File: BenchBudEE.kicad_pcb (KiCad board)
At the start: 4 copper layers, 165.1 x 63.5 mm, 67 parts, among them K1 1461069-5, P1 24 Pin MiniFit JR, P2 CONN_3X2, P3 CONN_2, P4 12 Pin Terminal Block, P5 3 Pin TB, Q1 2N3904, Q2 DMN65D8L-7, Q3 AOD476, Q4 AOD476, U1 LTV-816S, U2 MCP3901, U3 LMT84, U4 OPA4170, U6 MCP4801

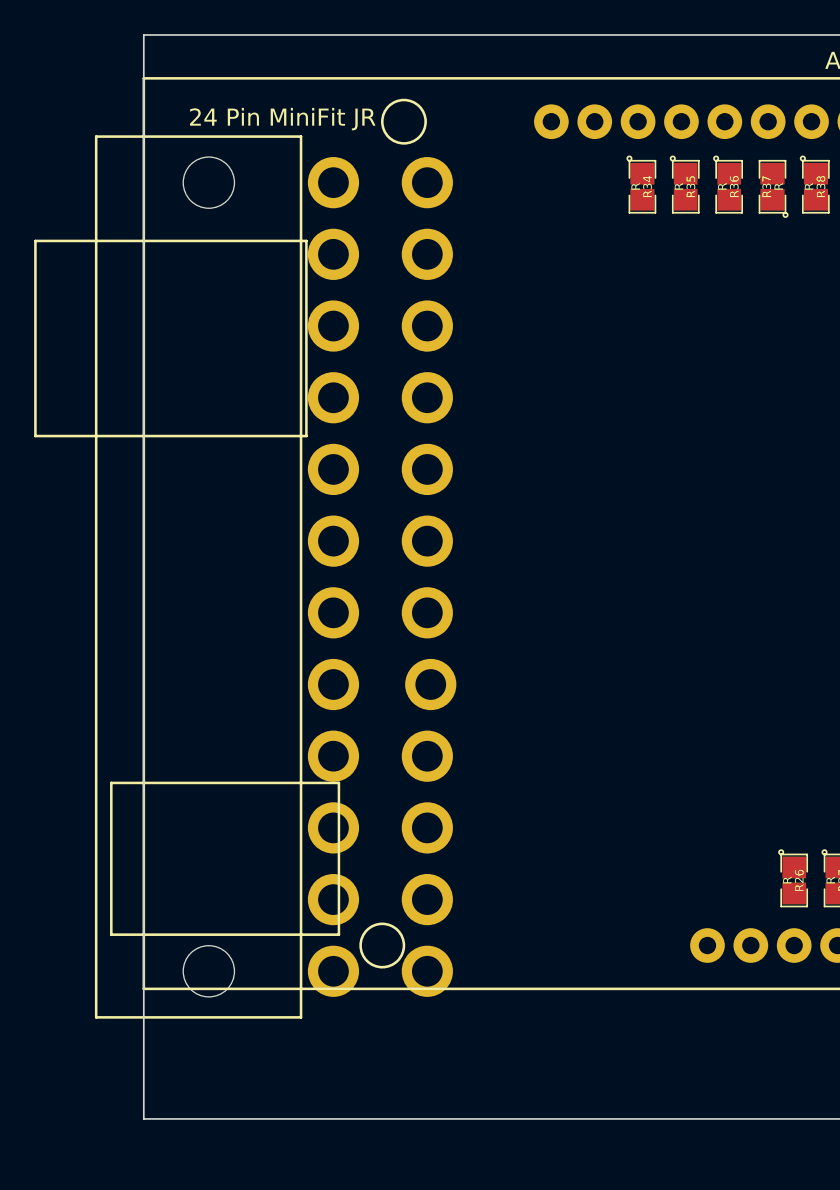
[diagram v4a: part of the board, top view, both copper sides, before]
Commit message: Power protection and filter: assc/placement
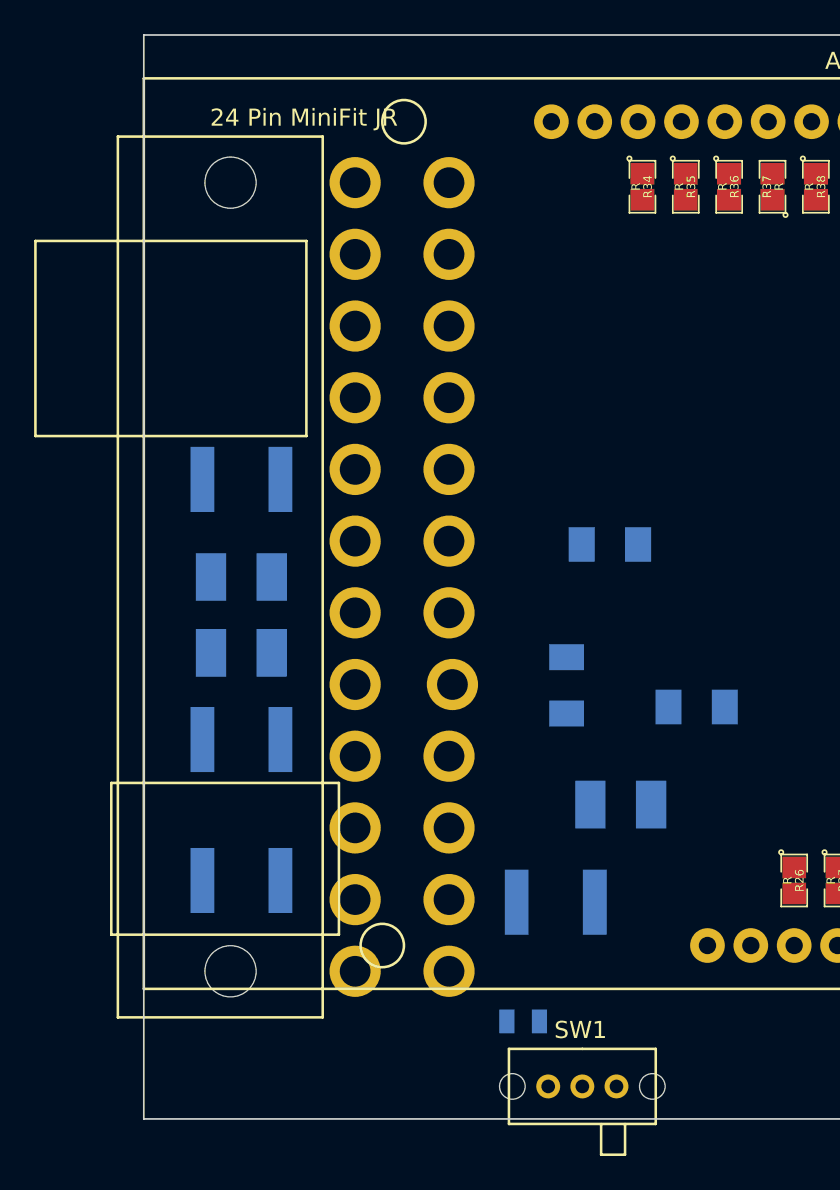
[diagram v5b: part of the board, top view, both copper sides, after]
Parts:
- added C2: C, SM1206, B.Cu at (149.2, 141.6)
- added C3: C, SM1206, B.Cu at (146.7, 149.9)
- added C4: C, SM1206, B.Cu at (154.3, 151.1)
- added L1: CM322522-220KL, SM1210L, B.Cu at (127.6, 148.0)
- added L2: CM322522-220KL, SM1210L, B.Cu at (127.6, 143.5)
- added L3: CM322522-220KL, SM1210L, B.Cu at (149.9, 156.8)
- added R14: R, SM0805, B.Cu at (144.1, 169.5)
- added SW1: Power Switch, BB_switch, F.Cu at (143.5, 173.4)
- added TH1: MINISMDC050F-2, SM1812, B.Cu at (127.6, 161.3)
- added TH2: MINISMDC050F-2, SM1812, B.Cu at (127.6, 153.0)
- added TH3: MINISMDC050F-2, SM1812, B.Cu at (127.6, 137.8)
- added TH4: MINISMDC050F-2, SM1812, B.Cu at (146.1, 162.6)
- moved P1 1.27 mm to (127.0, 143.5)

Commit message: Power Adjustment: assc/placement
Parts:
- added C14: C, SM0805, F.Cu at (189.9, 145.4)
- added C15: C, SM0805, F.Cu at (189.9, 127.0)
- added C16: C, SM0805, F.Cu at (156.8, 146.1)
- added C17: C, SM0805, F.Cu at (189.9, 140.3)
- added C18: C, SM0805, F.Cu at (189.9, 132.1)
- added C19: C, SM0805, F.Cu at (156.8, 128.3)
- added C20: C, SM0805, F.Cu at (189.9, 142.9)
- added C21: C, SM0805, F.Cu at (156.8, 141.0)
- added C22: C, SM0805, F.Cu at (189.9, 129.5)
- added C23: C, SM0805, F.Cu at (156.8, 133.3)
- added C24: C, SM0805, F.Cu at (156.8, 143.5)
- added C25: C, SM0805, F.Cu at (156.8, 130.8)
- added D10: MMBD914-7-F, SOT23-DIODE, B.Cu at (165.7, 127.6)
- added D11: MMBD914-7-F, SOT23-DIODE, B.Cu at (168.9, 142.2)
- added D12: MMBD914-7-F, SOT23-DIODE, B.Cu at (168.9, 132.1)
- added D3: MMBD914-7-F, SOT23-DIODE, B.Cu at (198.1, 125.7)
- added D6: MMBD914-7-F, SOT23-DIODE, B.Cu at (198.8, 146.1)
- added D7: MMBD914-7-F, SOT23-DIODE, B.Cu at (201.9, 141.6)
- added D8: MMBD914-7-F, SOT23-DIODE, B.Cu at (165.7, 146.7)
- added D9: MMBD914-7-F, SOT23-DIODE, B.Cu at (201.9, 130.8)
- added R18: 5K, EVUE3K, F.Cu at (196.8, 167.6)
- added R19: R, SM0805, B.Cu at (197.5, 141.6)
- added R20: R, SM0805, F.Cu at (192.4, 137.8)
- added R21: 715, SM0805, B.Cu at (164.5, 142.2)
- added R22: R, SM0805, F.Cu at (213.4, 118.7)
- added R23: R, SM0805, F.Cu at (213.4, 121.3)
- added R24: R, SM0805, F.Cu at (221.6, 118.7)
- added R25: R, SM0805, F.Cu at (221.6, 121.3)
- added R50: R, SM0805, F.Cu at (177.8, 120.7)
- added R51: R, SM0805-blob, F.Cu at (180.3, 120.7)
- added R52: R, SM0805, F.Cu at (192.4, 134.6)
- added R53: R, SM0805, B.Cu at (197.5, 130.8)
- added R54: 715, SM0805, B.Cu at (164.5, 132.1)
- added R55: 5K, EVUE3K, F.Cu at (196.2, 119.4)
- added U10: LM337T, TO220, F.Cu at (161.3, 130.8)
- added U7: LM317, TO220, F.Cu at (194.3, 142.9)
- added U8: LM317, TO220, F.Cu at (161.3, 143.5)
- added U9: LM337T, TO220, F.Cu at (194.3, 129.5)
- moved P3 9.86 mm to (207.6, 158.8)
- moved C1 5.08 mm to (221.6, 157.5)
- moved C12 5.08 mm to (214.0, 171.4)
- moved C13 5.08 mm to (245.1, 167.0)
- moved C7 5.08 mm to (214.0, 157.5)
- moved D5 5.08 mm to (255.3, 171.4)
- moved Q2 5.08 mm to (224.2, 167.0)
- moved Q3 5.08 mm to (261.0, 165.7)
- moved Q4 5.08 mm to (252.1, 165.7)
- moved R11 5.08 mm to (238.1, 152.4)
- moved R45 5.08 mm to (235.6, 148.6)
- moved R8 5.08 mm to (238.1, 158.8)
- moved R9 5.08 mm to (241.9, 158.8)
- moved U2 5.08 mm to (214.0, 156.2)
- moved U6 5.08 mm to (214.0, 166.4)
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
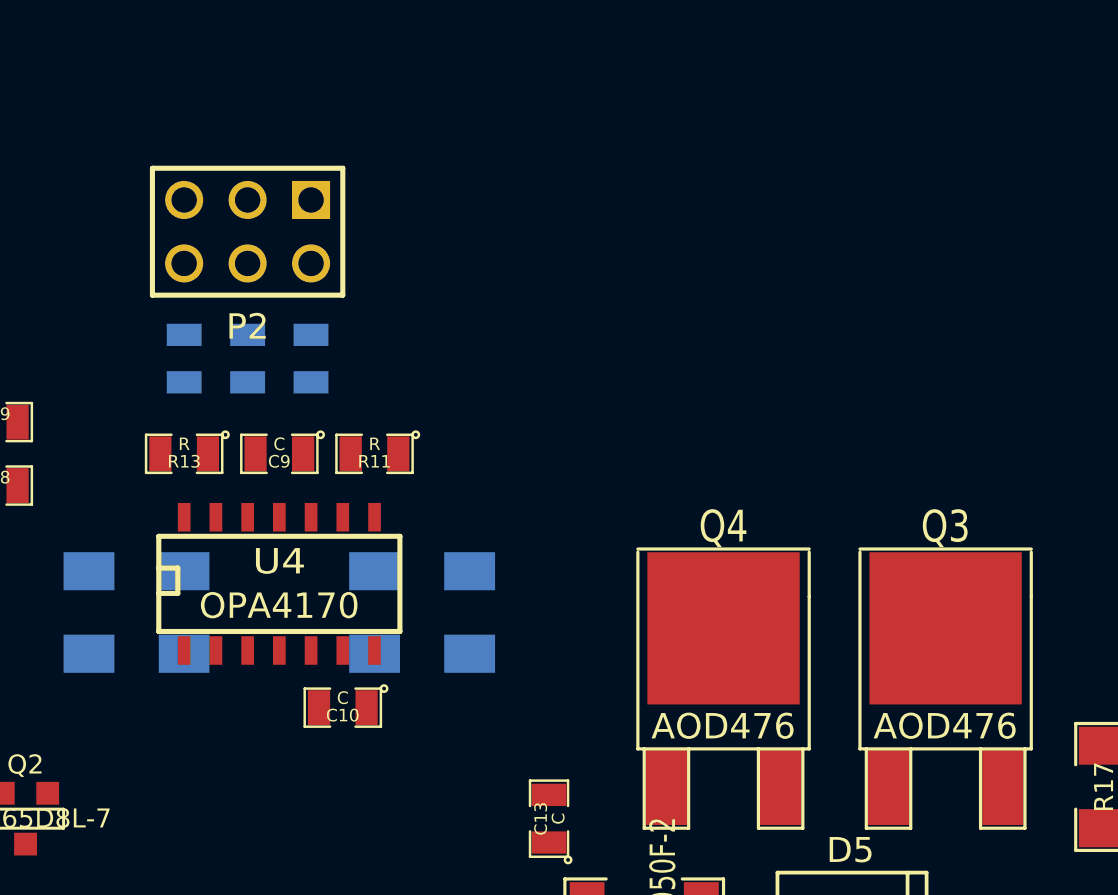
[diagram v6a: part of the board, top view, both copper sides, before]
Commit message: LED driver: assc/placement
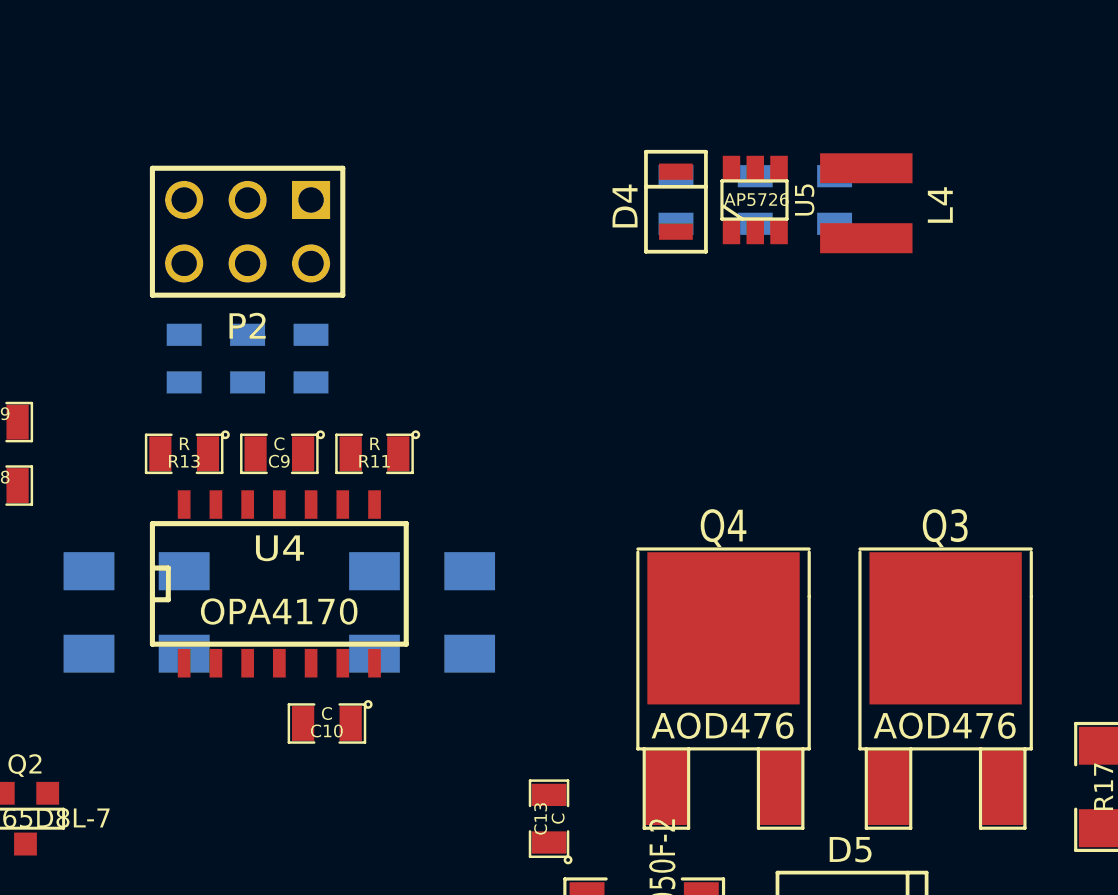
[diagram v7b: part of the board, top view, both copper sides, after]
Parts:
- added C5: 1u, SM0805, B.Cu at (250.2, 142.2)
- added C6: 1u, SM0805, B.Cu at (253.4, 142.2)
- added D4: B0540WS-7, SOD-323, F.Cu at (250.2, 143.5)
- added L4: NR4012T220M, NR4012, F.Cu at (257.8, 141.0)
- added R15: 15R, SM0805, B.Cu at (256.5, 142.2)
- added U5: AP5726, SOT23_6, F.Cu at (253.4, 142.2)
- U4: footprint SO14E -> SO14N
- moved C10 0.90 mm to (236.2, 163.2)
